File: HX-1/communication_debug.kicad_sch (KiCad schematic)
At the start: 28 parts, among them J1 USB_C_Receptacle_USB2.0_16P, U2 USBLC6-2SC6, U4 LSM6DS3

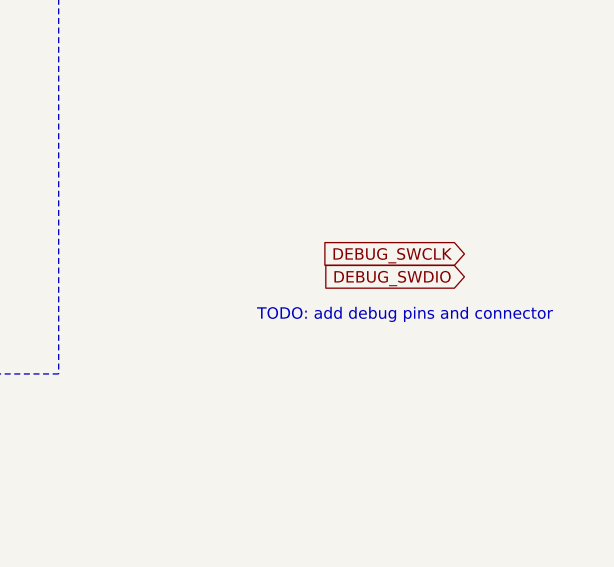
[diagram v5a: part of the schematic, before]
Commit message: remove fdcan connector for space, add header debug pin
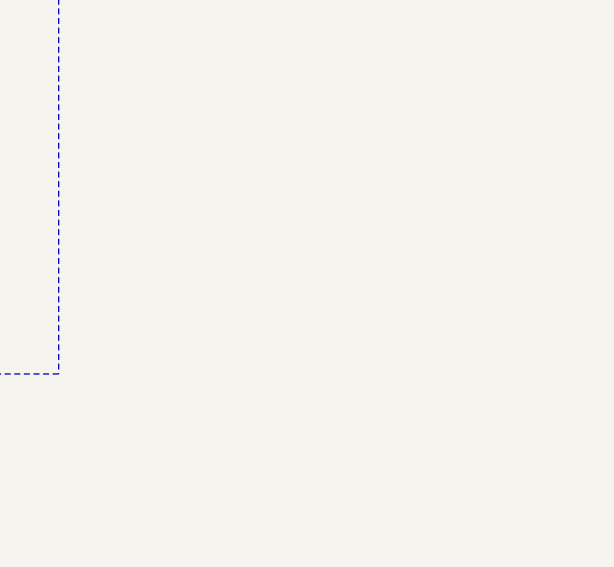
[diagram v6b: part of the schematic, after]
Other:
- note removed: "TODO: add debug pins and connector"
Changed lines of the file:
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@@
-		)
-	)
-	(text "TODO: add debug pins and connector"
-		(exclude_from_sim no)
-		(at 265.176 136.398 0)
-		(effects
-			(font
-				(size 1.27 1.27)
-			)
 		)
 	)
@@
 		)
 	)
-	(global_label "DEBUG_SWDIO"
-		(shape input)
-		(at 271.78 132.08 180)
-		(fields_autoplaced yes)
-		(effects
-			(font
-				(size 1.27 1.27)
-			)
-			(justify right)
-		)
-		(property "Intersheetrefs" "${INTERSHEET_REFS}"
-			(at 255.6715 132.08 0)
-			(effects
-				(font
-					(size 1.27 1.27)
-				)
-				(justify right)
-				(hide yes)
-			)
-		)
-	)
 	(global_label "USB_VBUS_SENSE"
 		(shape input)
@@
 				(hide yes)
 			)
-		)
-	)
-	(global_label "DEBUG_SWCLK"
-		(shape input)
-		(at 271.78 129.54 180)
-		(fields_autoplaced yes)
-		(effects
-			(font
-				(size 1.27 1.27)
-			)
-			(justify right)
-		)
-		(property "Intersheetrefs" "${INTERSHEET_REFS}"
-			(at 255.3087 129.54 0)
-			(effects
-				(font
-					(size 1.27 1.27)
-				)
-				(justify right)
-				(hide yes)
-			)

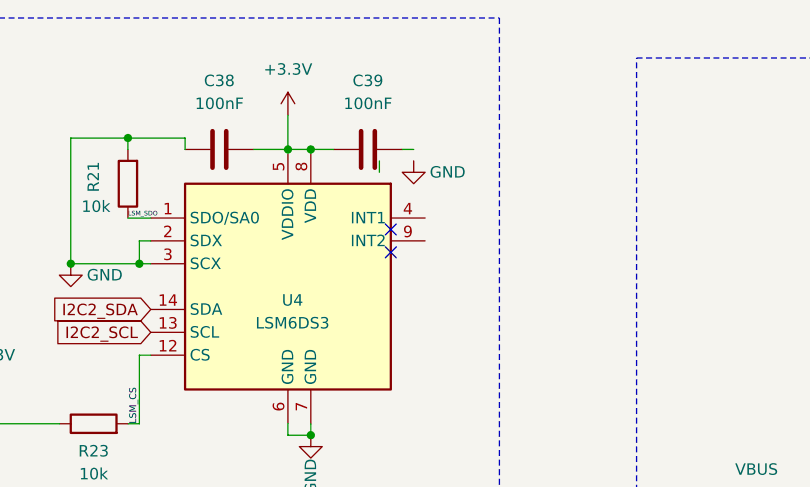
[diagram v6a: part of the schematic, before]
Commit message: increase board height to 90mm to give more space to jst connectors
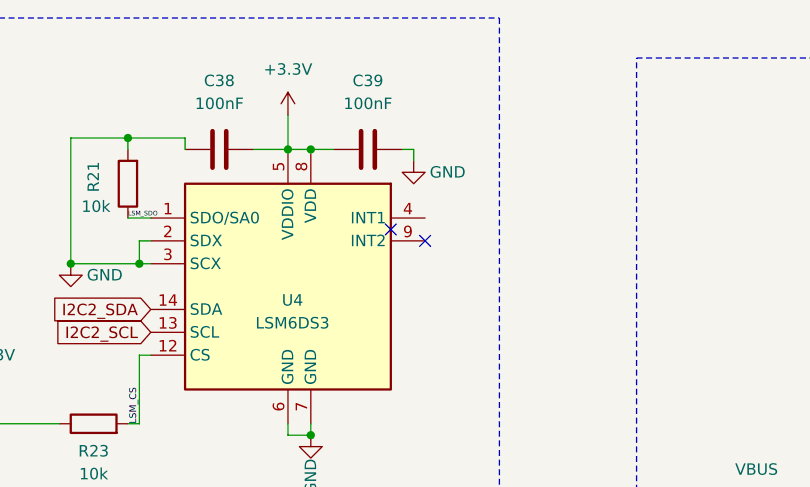
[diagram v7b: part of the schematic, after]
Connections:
- net GND: now also C39.2
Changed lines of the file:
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@@
 	)
 	(no_connect
-		(at 68.58 40.64)
+		(at 72.39 39.37)
 	)
 	(no_connect
@@
 	(wire
 		(pts
+			(xy 71.12 29.21) (xy 71.12 30.48)
+		)
+		(stroke
+			(width 0)
+			(type default)
+		)
+	)
+	(wire
+		(pts
 			(xy 25.4 154.94) (xy 30.48 154.94)
 		)
@@
 		)
 		(stroke
-			(width 0)
-			(type default)
-		)
-	)
-	(wire
-		(pts
-			(xy 67.31 31.75) (xy 67.31 30.48)
-		)
-		(stroke

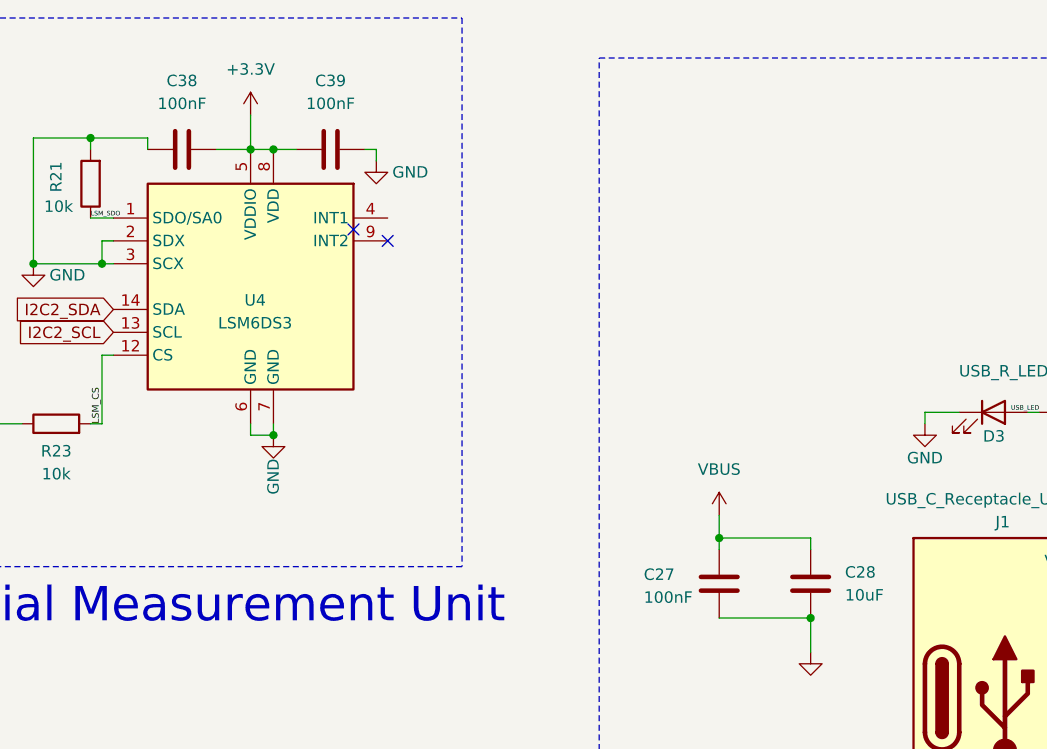
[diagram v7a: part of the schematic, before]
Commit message: renumber capacitors, position all MCU caps
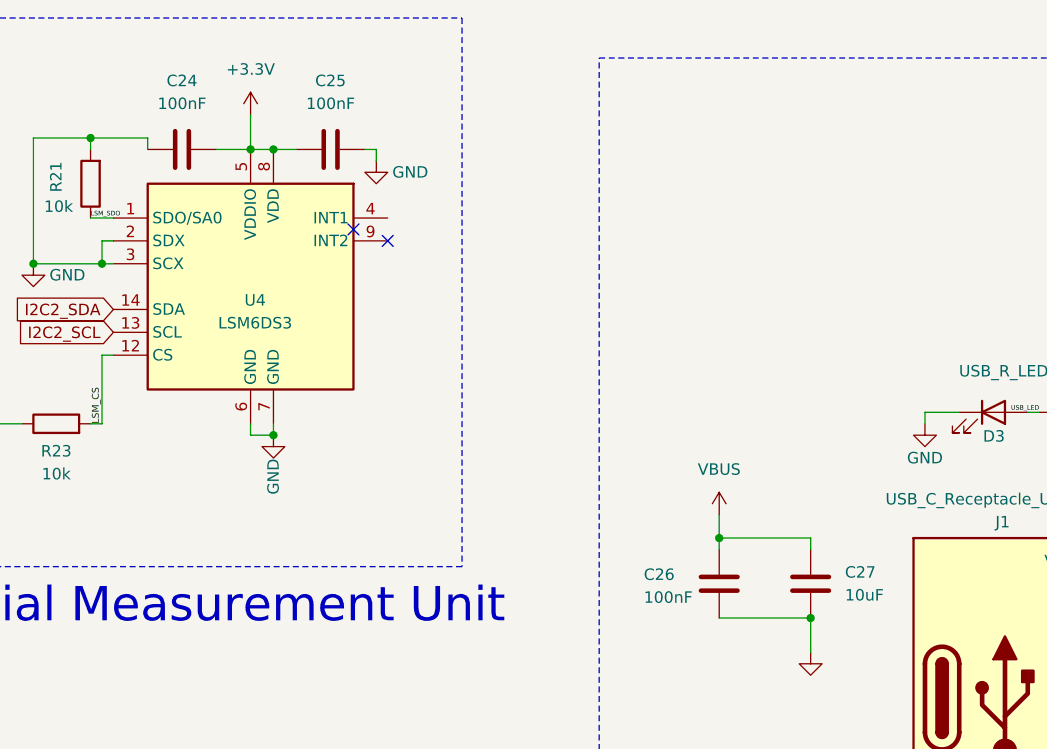
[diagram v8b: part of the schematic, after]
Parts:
- renumbered C38 to C24, C39 to C25, C27 to C26, C28 to C27
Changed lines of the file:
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@@
 		(dnp no)
 		(fields_autoplaced yes)
-		(property "Reference" "C39"
+		(property "Reference" "C25"
 			(at 66.04 21.59 90)
 			(effects
@@
 			(project "HX-1"
 				(path "/a3219989-2bf1-44ea-9412-fab86edfb39b/f68304e7-586c-4481-9c91-394c7e636be5"
-					(reference "C39")
+					(reference "C25")
 					(unit 1)
 				)
@@
 		(dnp no)
 		(fields_autoplaced yes)
-		(property "Reference" "C28"
+		(property "Reference" "C27"
 			(at 123.19 76.1999 0)
 			(effects
@@
 			(project "HX-1"
 				(path "/a3219989-2bf1-44ea-9412-fab86edfb39b/f68304e7-586c-4481-9c91-394c7e636be5"
-					(reference "C28")
+					(reference "C27")
 					(unit 1)
 				)
@@
 		(dnp no)
 		(fields_autoplaced yes)
-		(property "Reference" "C38"
+		(property "Reference" "C24"
 			(at 49.53 21.59 90)
 			(effects
@@
 			(project "HX-1"
 				(path "/a3219989-2bf1-44ea-9412-fab86edfb39b/f68304e7-586c-4481-9c91-394c7e636be5"
-					(reference "C38")
+					(reference "C24")
 					(unit 1)
 				)
@@
 		(on_board yes)
 		(dnp no)
-		(property "Reference" "C27"
+		(property "Reference" "C26"
 			(at 100.838 76.454 0)
 			(effects
@@
 			(project "HX-1"
 				(path "/a3219989-2bf1-44ea-9412-fab86edfb39b/f68304e7-586c-4481-9c91-394c7e636be5"
-					(reference "C27")
-					(unit 1)
-				)
+					(reference "C26")
+					(unit 1)
+				)
